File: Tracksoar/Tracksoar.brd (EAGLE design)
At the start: 50.4 x 19.5 mm, 35 parts, among them IC2 74AHC1G125DBV, U1 ATMEGA328P, Y1 16MHZ

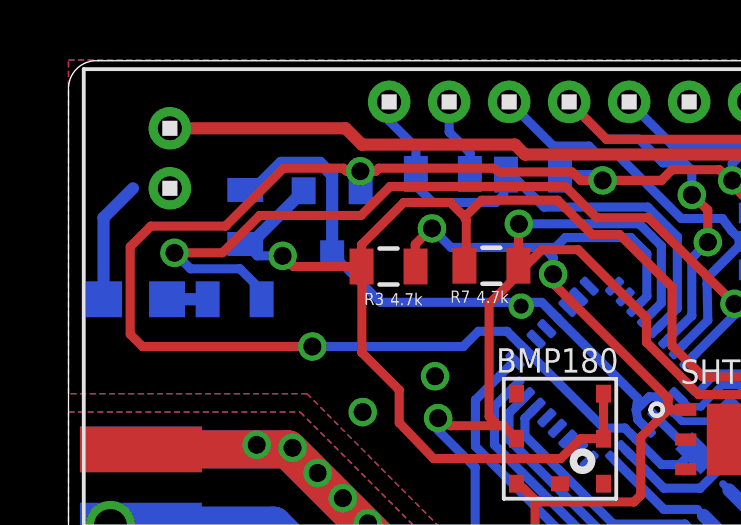
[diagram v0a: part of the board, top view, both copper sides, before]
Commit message: Added V1.1 board layout
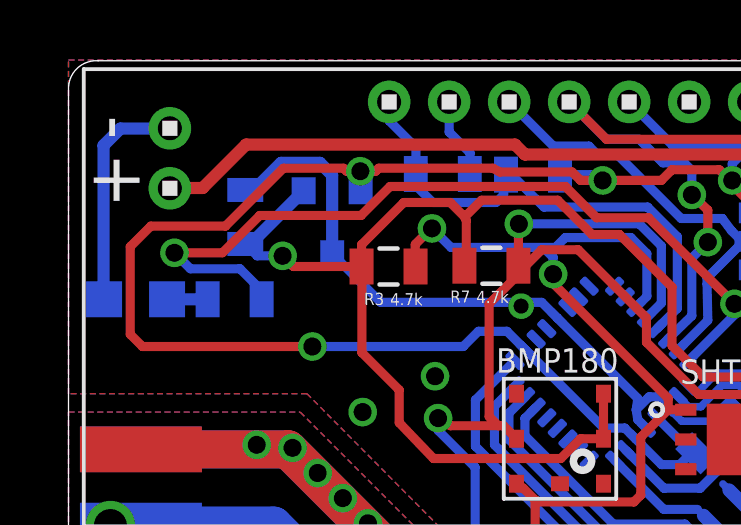
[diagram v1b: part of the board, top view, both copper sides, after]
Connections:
- net 15V: now also U$3.1; no longer U$3.2
- net GND: now also U$3.2; no longer U$3.1
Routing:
- net GND: track 77.7 -> 81.2 mm
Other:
- board text added: "Tracksoar v1.1"
- board text removed: "Tracksoar v1"
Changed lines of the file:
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@@
 <?xml version="1.0" encoding="utf-8"?>
 <!DOCTYPE eagle SYSTEM "eagle.dtd">
-<eagle version="7.3.0">
+<eagle version="7.5.0">
 <drawing>
 <settings>
@@
 <board>
 <plain>
-<text x="31.6484" y="4.2926" size="0.8128" layer="26" rot="MR180">Tracksoar v1</text>
+<text x="31.6484" y="4.2926" size="0.8128" layer="26" rot="MR180">Tracksoar v1.1</text>
 <text x="38.1" y="2.6924" size="0.6096" layer="26" rot="MR0">&lt;3 Swiss</text>
-<text x="0.9144" y="16.8402" size="1.778" layer="26">+</text>
-<text x="2.286" y="14.8082" size="1.778" layer="26" rot="R90">-</text>
+<text x="0.8636" y="14.6558" size="1.778" layer="25" rot="MR90">+</text>
+<text x="2.5908" y="17.7292" size="1.778" layer="25" rot="MR270">-</text>
 <text x="23.8506" y="16.6116" size="0.8128" layer="26" rot="MR90">GND</text>
 <text x="21.209" y="15.9258" size="0.8128" layer="26" rot="MR0">FTDI</text>
@@
 <contactref element="LM3480" pad="3"/>
 <contactref element="BMP180" pad="7"/>
-<wire x1="2.175" y1="15.3068" x2="1.1938" y2="14.3256" width="0.4064" layer="16"/>
-<wire x1="1.1938" y1="14.3256" x2="1.1938" y2="11.6246" width="0.4064" layer="16"/>
+<wire x1="1.1938" y1="16.7386" x2="1.1938" y2="11.6246" width="0.4064" layer="16"/>
 <wire x1="1.1938" y1="11.6246" x2="1.2106" y2="11.6078" width="0.4064" layer="16"/>
 <wire x1="5.8624" y1="15.3068" x2="5.9182" y2="15.251" width="0.4064" layer="16"/>
@@
 <contactref element="FTDI" pad="1"/>
 <contactref element="FTDI" pad="2"/>
-<contactref element="U$3" pad="1"/>
 <wire x1="32.004" y1="10.4602" x2="32.004" y2="9.398" width="0.3048" layer="1"/>
 <wire x1="32.004" y1="9.398" x2="31.369" y2="8.7376" width="0.3048" layer="1"/>
@@
 <via x="10.0076" y="4.1402" extent="1-16" drill="0.6"/>
 <via x="10.8458" y="3.302" extent="1-16" drill="0.6"/>
+<contactref element="U$3" pad="2"/>
+<wire x1="1.1938" y1="16.7386" x2="1.7526" y2="17.2974" width="0.4064" layer="16"/>
+<wire x1="1.7526" y1="17.2974" x2="3.3942" y2="17.2974" width="0.4064" layer="16"/>
+<wire x1="3.3942" y1="17.2974" x2="3.4036" y2="17.3068" width="0.4064" layer="16"/>
 <wire x1="9.8298" y1="7.8486" x2="8.3312" y2="5.8166" width="0" layer="19" extent="1-1"/>
 </signal>
@@
 </signal>
 <signal name="15V">
-<wire x1="9.2616" y1="17.3068" x2="9.8044" y2="16.764" width="0.4064" layer="1"/>
-<wire x1="9.8044" y1="16.764" x2="14.9098" y2="16.764" width="0.4064" layer="1"/>
+<wire x1="5.9436" y1="16.764" x2="14.9098" y2="16.764" width="0.4064" layer="1"/>
 <wire x1="14.9098" y1="16.764" x2="15.24" y2="16.4338" width="0.4064" layer="1"/>
 <wire x1="15.24" y1="16.4338" x2="22.606" y2="16.4338" width="0.4064" layer="1"/>
@@
 <wire x1="28.4734" y1="13.1514" x2="30.9628" y2="13.1514" width="0.4064" layer="1"/>
 <wire x1="30.9628" y1="13.1514" x2="31.054" y2="13.0602" width="0.4064" layer="1"/>
-<contactref element="U$3" pad="2"/>
-<wire x1="9.2616" y1="17.3068" x2="3.4036" y2="17.3068" width="0.4064" layer="1"/>
 <wire x1="31.104" y1="14.6558" x2="31.104" y2="13.1102" width="0.4064" layer="1"/>
 <wire x1="31.104" y1="13.1102" x2="31.054" y2="13.0602" width="0.4064" layer="1"/>
+<contactref element="U$3" pad="1"/>
+<wire x1="5.9436" y1="16.764" x2="4.4958" y2="15.3162" width="0.4064" layer="1"/>
+<wire x1="4.4958" y1="15.3162" x2="3.413" y2="15.3162" width="0.4064" layer="1"/>
+<wire x1="3.413" y1="15.3162" x2="3.4036" y2="15.3068" width="0.4064" layer="1"/>
 </signal>
 <signal name="N$9">

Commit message: Added V1.2 board
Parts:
- removed BMP180: BMP180, SparkFun-Sensors:BMP180
- removed SHT21: SHT21, sht21:DFN300X300X110-7N
- added IC1: BME280, bosch-bme280:BME280
- added R2: 4.7k, SparkFun-Resistors:0805
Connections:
- new net N$2: IC1.2, R2.2
- net 3V: now also IC1.6, IC1.8, R2.1; no longer BMP180.2, BMP180.3, SHT21.5
- net GND: now also IC1.1, IC1.5, IC1.7; no longer BMP180.7, SHT21.2
- net SCL: now also IC1.4; no longer BMP180.5, SHT21.6
- net SDA: now also IC1.3; no longer BMP180.6, SHT21.1
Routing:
- net 3V: track 76.8 -> 66.9 mm
- net SCL: track 35.9 -> 27.9 mm
- net SDA: track 30.1 -> 25.3 mm
- net N$2: track 0.00 -> 4.17 mm

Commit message: Soldermasked Vias and minor layout fixes
solder masked vias to resolve soldering issues. Removed separated
ground around RF output. Updated silkscreen to read v1.2 and prevent
clipping of the L2 designator and value. Removed unnecessary ground
vias. Fixed floating ground on BME280 sensor.
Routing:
- net GND: track 81.2 -> 83.6 mm, vias 58 -> 55
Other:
- board text added: "Tracksoar v1.2"
- board text removed: "Tracksoar v1.1"
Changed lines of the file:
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@@
 <?xml version="1.0" encoding="utf-8"?>
 <!DOCTYPE eagle SYSTEM "eagle.dtd">
-<eagle version="7.3.0">
+<eagle version="7.5.0">
 <drawing>
 <settings>
@@
 <board>
 <plain>
-<text x="31.6484" y="4.2926" size="0.8128" layer="26" rot="MR180">Tracksoar v1.1</text>
+<text x="31.6484" y="4.2926" size="0.8128" layer="26" rot="MR180">Tracksoar v1.2</text>
 <text x="38.1" y="2.6924" size="0.6096" layer="26" rot="MR0">&lt;3 Swiss</text>
 <text x="0.8636" y="14.6558" size="1.778" layer="25" rot="MR90">+</text>
@@
 </class>
 </classes>
-<designrules name="oshpark-2layer">
+<designrules name="oshpark-2layer *">
 <description language="de">&lt;b&gt;EAGLE Design Rules&lt;/b&gt;
 &lt;p&gt;
@@
 <param name="mlMinCreamFrame" value="0mil"/>
 <param name="mlMaxCreamFrame" value="0mil"/>
-<param name="mlViaStopLimit" value="0mil"/>
+<param name="mlViaStopLimit" value="30mil"/>
 <param name="srRoundness" value="0"/>
 <param name="srMinRoundness" value="0mil"/>
@@
 </element>
 <element name="L2" library="resistor" package="L1812" value="2.2uh" x="28.4734" y="11.2014" smashed="yes" rot="R270">
-<attribute name="NAME" x="25.4762" y="6.6802" size="0.8128" layer="25"/>
-<attribute name="VALUE" x="29.8196" y="7.747" size="0.8128" layer="25" rot="R180"/>
+<attribute name="NAME" x="26.7462" y="7.0358" size="0.8128" layer="25"/>
+<attribute name="VALUE" x="29.4386" y="6.6802" size="0.8128" layer="25" rot="R180"/>
 </element>
 <element name="R8" library="SparkFun-Resistors" package="0805" value="1m" x="32.004" y="14.6558" smashed="yes" rot="R180">
@@
 <contactref element="C8" pad="2"/>
 <contactref element="C7" pad="2"/>
-<via x="29.8704" y="5.588" extent="1-16" drill="0.6"/>
-<via x="9.8298" y="7.8486" extent="1-16" drill="0.6"/>
-<via x="15.113" y="11.3792" extent="1-16" drill="0.5"/>
-<via x="12.2428" y="9.0424" extent="1-16" drill="0.6"/>
 <via x="1.4224" y="1.524" extent="1-16" drill="1.1" shape="square"/>
 <via x="24.4602" y="3.3528" extent="1-16" drill="0.6"/>
@@
 <vertex x="40.259" y="3.7592"/>
 <vertex x="40.259" y="0.0254"/>
-<vertex x="12.573" y="0.0254"/>
-<vertex x="12.6238" y="3.7846"/>
-<vertex x="7.9756" y="8.4582"/>
+<vertex x="0.0254" y="0.0254"/>
+<vertex x="0.0762" y="4.699"/>
 <vertex x="0.0254" y="8.4582"/>
 </polygon>
@@
 <vertex x="40.259" y="3.7592"/>
 <vertex x="40.259" y="0.0254"/>
-<vertex x="12.573" y="0.0254"/>
-<vertex x="12.6238" y="3.7846"/>
-<vertex x="7.9756" y="8.4582"/>
+<vertex x="0.0254" y="0.0254"/>
+<vertex x="0.0762" y="4.7752"/>
 <vertex x="0.0254" y="8.4582"/>
-</polygon>
-<polygon width="0.4064" layer="16">
-<vertex x="0.0254" y="7.8486"/>
-<vertex x="7.747" y="7.8486"/>
-<vertex x="12.0142" y="3.5814"/>
-<vertex x="12.0142" y="0.0254"/>
-<vertex x="0.0254" y="0.0254"/>
-</polygon>
-<polygon width="0.4064" layer="1">
-<vertex x="0.0254" y="7.8486"/>
-<vertex x="7.747" y="7.8486"/>
-<vertex x="12.0142" y="3.5814"/>
-<vertex x="12.0142" y="0.0254"/>
-<vertex x="0.0254" y="0.0254"/>
 </polygon>
 <wire x1="5.6134" y1="1.4986" x2="5.6388" y2="1.4986" width="0.4064" layer="1"/>
@@
 <contactref element="IC1" pad="1"/>
 <contactref element="IC1" pad="5"/>
-<wire x1="9.8298" y1="7.8486" x2="8.3312" y2="5.8166" width="0" layer="19" extent="1-1"/>
-<wire x1="16.0176" y1="7.9338" x2="17.3176" y2="7.9338" width="0" layer="19" extent="1-1"/>
+<via x="5.1816" y="6.731" extent="1-16" drill="0.6"/>
+<wire x1="16.0176" y1="7.9338" x2="16.0176" y2="7.5536" width="0.3048" layer="1"/>
+<wire x1="16.0176" y1="7.5536" x2="16.2306" y2="7.3406" width="0.3048" layer="1"/>
+<wire x1="16.2306" y1="7.3406" x2="17.2466" y2="7.3406" width="0.3048" layer="1"/>
+<wire x1="17.2466" y1="7.3406" x2="17.2974" y2="7.2898" width="0.3048" layer="1"/>
+<wire x1="17.2974" y1="7.2898" x2="17.2974" y2="7.9136" width="0.3048" layer="1"/>
+<wire x1="17.2974" y1="7.9136" x2="17.3176" y2="7.9338" width="0.3048" layer="1"/>
 </signal>
 <signal name="VCC">

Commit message: BME280 Decoupling Cap
Added a 100nf decoupling cap next to the bme280
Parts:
- added C6: 100nf, SparkFun-Capacitors:0805
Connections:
- net 3V: now also C6.2
- net GND: now also C6.1
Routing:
- net 3V: track 66.9 -> 68.2 mm
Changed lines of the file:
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@@
 <element name="IC1" library="bosch-bme280" package="BME280" value="BME280" x="16.9926" y="6.9088"/>
 <element name="R2" library="SparkFun-Resistors" package="0805" value="4.7k" x="20.066" y="6.8834" rot="R270"/>
+<element name="C6" library="SparkFun-Capacitors" package="0805" value="100nf" x="18.1356" y="10.9728" rot="R270"/>
 </elements>
 <signals>
@@
 <wire x1="17.2974" y1="7.2898" x2="17.2974" y2="7.9136" width="0.3048" layer="1"/>
 <wire x1="17.2974" y1="7.9136" x2="17.3176" y2="7.9338" width="0.3048" layer="1"/>
+<contactref element="C6" pad="1"/>
 </signal>
 <signal name="VCC">
@@
 <wire x1="20.066" y1="7.7834" x2="20.066" y2="7.8994" width="0.3048" layer="1"/>
 <wire x1="20.066" y1="7.8994" x2="21.1836" y2="9.017" width="0.3048" layer="1"/>
+<contactref element="C6" pad="2"/>
+<wire x1="18.1356" y1="10.0728" x2="18.1356" y2="9.3472" width="0.3048" layer="1"/>
+<wire x1="18.1356" y1="9.3472" x2="17.6784" y2="8.89" width="0.3048" layer="1"/>
 </signal>
 <signal name="N$1">

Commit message: v2 BME280 decoupling cap
added decoupling cap to bme280 of v2 board.
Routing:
- net SDA: track 25.3 -> 26.7 mm, vias 2 -> 3
- net SCL: track 27.9 -> 26.9 mm
- net GND: vias 55 -> 54
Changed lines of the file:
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@@
 <contactref element="C7" pad="2"/>
 <via x="1.4224" y="1.524" extent="1-16" drill="1.1" shape="square"/>
-<via x="24.4602" y="3.3528" extent="1-16" drill="0.6"/>
 <wire x1="19.99743125" y1="8.012628125" x2="20.466259375" y2="7.5438" width="0.254" layer="16"/>
 <wire x1="20.466259375" y1="7.5438" x2="21.717" y2="7.5438" width="0.254" layer="16"/>
@@
 <contactref element="SPI/I2C" pad="2"/>
 <contactref element="IC1" pad="3"/>
-<wire x1="16.6676" y1="5.8838" x2="16.6676" y2="2.5476" width="0.3048" layer="1"/>
-<wire x1="16.6676" y1="2.5476" x2="15.58" y2="1.46" width="0.3048" layer="1"/>
 <wire x1="16.6676" y1="5.8838" x2="16.6676" y2="6.5734" width="0.3048" layer="1"/>
 <wire x1="16.6676" y1="6.5734" x2="16.4592" y2="6.7818" width="0.3048" layer="1"/>
@@
 <wire x1="15.2146" y1="10.0584" x2="16.1798" y2="11.0236" width="0.3048" layer="1"/>
 <wire x1="16.1798" y1="11.0236" x2="16.1798" y2="12.446" width="0.3048" layer="1"/>
+<wire x1="16.6676" y1="5.8838" x2="16.6676" y2="5.3392" width="0.3048" layer="1"/>
+<wire x1="16.6676" y1="5.3392" x2="16.4592" y2="5.1308" width="0.3048" layer="1"/>
+<wire x1="16.4592" y1="5.1308" x2="15.494" y2="5.1308" width="0.3048" layer="1"/>
+<wire x1="15.494" y1="5.1308" x2="14.6304" y2="4.2672" width="0.3048" layer="1"/>
+<via x="14.6304" y="4.2672" extent="1-16" drill="0.6"/>
+<wire x1="14.6304" y1="4.2672" x2="14.6304" y2="2.9718" width="0.3048" layer="16"/>
+<wire x1="14.6304" y1="2.9718" x2="15.5956" y2="2.0066" width="0.3048" layer="16"/>
+<wire x1="15.5956" y1="2.0066" x2="15.5956" y2="1.4756" width="0.3048" layer="16"/>
+<wire x1="15.5956" y1="1.4756" x2="15.58" y2="1.46" width="0.3048" layer="16"/>
 </signal>
 <signal name="SCL">
@@
 <wire x1="13.5796" y1="1.4604" x2="13.58" y2="1.46" width="0.3048" layer="16"/>
 <contactref element="IC1" pad="4"/>
-<wire x1="16.0176" y1="5.8838" x2="16.0176" y2="3.8976" width="0.3048" layer="1"/>
-<wire x1="16.0176" y1="3.8976" x2="13.58" y2="1.46" width="0.3048" layer="1"/>
 <wire x1="12.3444" y1="7.6454" x2="12.446" y2="7.6454" width="0.3048" layer="1"/>
 <wire x1="12.446" y1="7.6454" x2="13.6652" y2="8.8646" width="0.3048" layer="1"/>
 <wire x1="13.6652" y1="8.8646" x2="13.6652" y2="11.3682" width="0.3048" layer="1"/>
 <wire x1="13.6652" y1="11.3682" x2="15.0224" y2="12.7254" width="0.3048" layer="1"/>
+<wire x1="16.0176" y1="5.8838" x2="14.106" y2="5.8838" width="0.3048" layer="1"/>
+<wire x1="14.106" y1="5.8838" x2="12.3444" y2="7.6454" width="0.3048" layer="1"/>
 </signal>
 <signal name="15V">
